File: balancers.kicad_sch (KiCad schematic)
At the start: 0 parts

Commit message: schematic: Cleanup
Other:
- company: (none) -> York Formula Student
- title: (none) -> Battery Management System
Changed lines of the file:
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@@
 	(generator_version "8.0")
 	(paper "A4")
+	(title_block
+		(title "Battery Management System")
+		(date "2025-02-08")
+		(rev "1")
+		(company "York Formula Student")
+	)
 	(wire
 		(pts

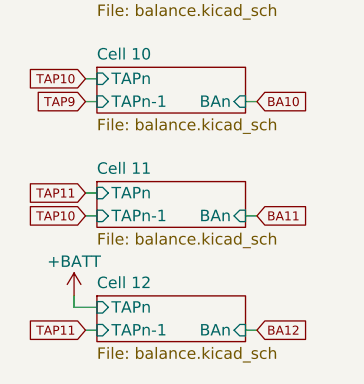
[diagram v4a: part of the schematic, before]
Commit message: schematic: Don't make CV12 go through fuse and adjust thermistor pinout
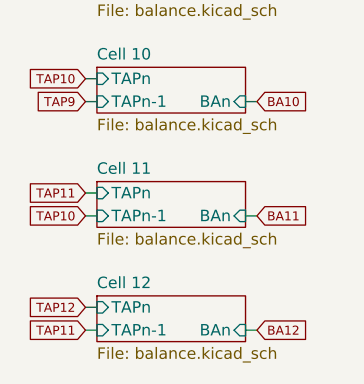
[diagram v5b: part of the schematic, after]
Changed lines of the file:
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@@
 	(wire
 		(pts
-			(xy 35.56 163.83) (xy 38.1 163.83)
+			(xy 36.83 163.83) (xy 38.1 163.83)
 		)
 		(stroke
@@
 	(wire
 		(pts
-			(xy 35.56 163.83) (xy 35.56 162.56)
-		)
-		(stroke
-			(width 0)
-			(type default)
-		)
-	)
-	(wire
-		(pts
 			(xy 36.83 74.93) (xy 38.1 74.93)
 		)
@@
 				)
 				(justify left)
+				(hide yes)
+			)
+		)
+	)
+	(global_label "TAP12"
+		(shape input)
+		(at 36.83 163.83 180)
+		(fields_autoplaced yes)
+		(effects
+			(font
+				(size 1 1)
+			)
+			(justify right)
+		)
+		(property "Intersheetrefs" "${INTERSHEET_REFS}"
+			(at 29.9559 163.83 0)
+			(effects
+				(font
+					(size 1.27 1.27)
+				)
+				(justify right)
 				(hide yes)
 			)
@@
 					(unit 1)
 				)
-			)
-		)
-	)
-	(symbol
-		(lib_id "power:+BATT")
-		(at 35.56 162.56 0)
-		(unit 1)
-		(exclude_from_sim no)
-		(in_bom yes)
-		(on_board yes)
-		(dnp no)
-		(property "Reference" "#PWR056"
-			(at 35.56 166.37 0)
-			(effects
-				(font
-					(size 1.27 1.27)
-				)
-				(hide yes)
-			)
-		)
-		(property "Value" "+BATT"
-			(at 35.56 158.75 0)
-			(effects
-				(font
-					(size 1.27 1.27)
-				)
-			)
-		)
-		(property "Footprint" ""
-			(at 35.56 162.56 0)
-			(effects
-				(font
-					(size 1.27 1.27)
-				)
-				(hide yes)
-			)
-		)
-		(property "Datasheet" ""
-			(at 35.56 162.56 0)
-			(effects
-				(font
-					(size 1.27 1.27)
-				)
-				(hide yes)
-			)
-		)
-		(property "Description" "Power symbol creates a global label with name \"+BATT\""
-			(at 35.56 162.56 0)
-			(effects
-				(font
-					(size 1.27 1.27)
-				)
-				(hide yes)
-			)
-		)
-		(pin "1"
-		)
-		(instances
-			(project "bms"
-				(path "/ae4a7653-8e6d-4e05-b144-1e5e3b2092b7/28948f48-ac92-4ccf-aa29-40bfebbeebe0"
-					(reference "#PWR056")
-					(unit 1)
-				)
